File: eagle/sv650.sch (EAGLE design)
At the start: 25 parts

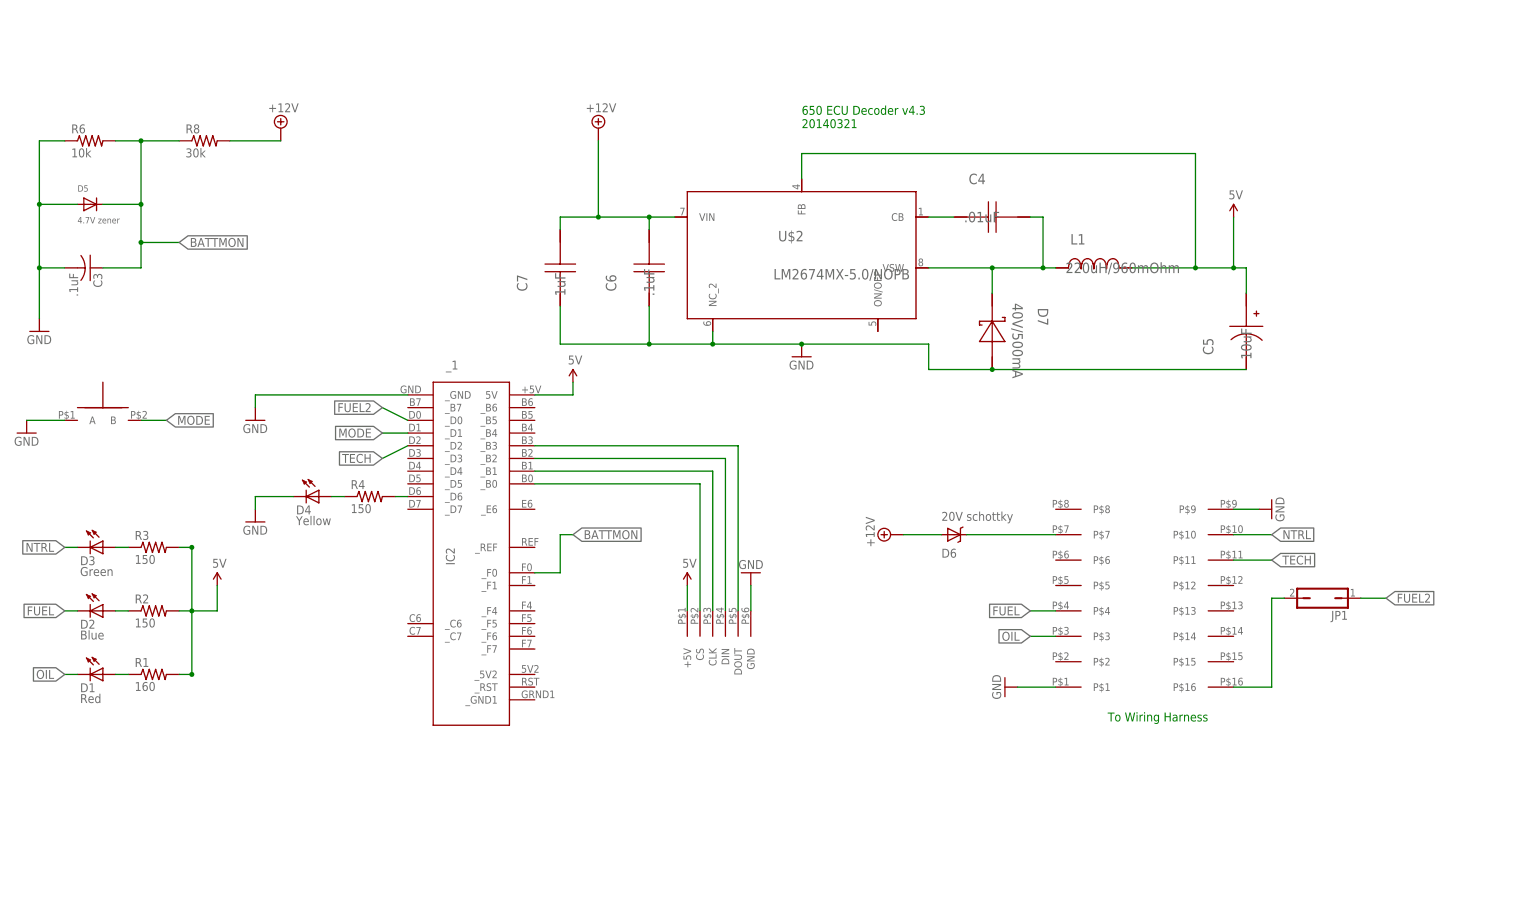
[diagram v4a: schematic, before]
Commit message: Fuel level LED is now controlled by Teensy     Use LT082CP to measure fuel sensor     add 5W 82ohm resistor to fuel line     Remove Fuel2 jumper/support
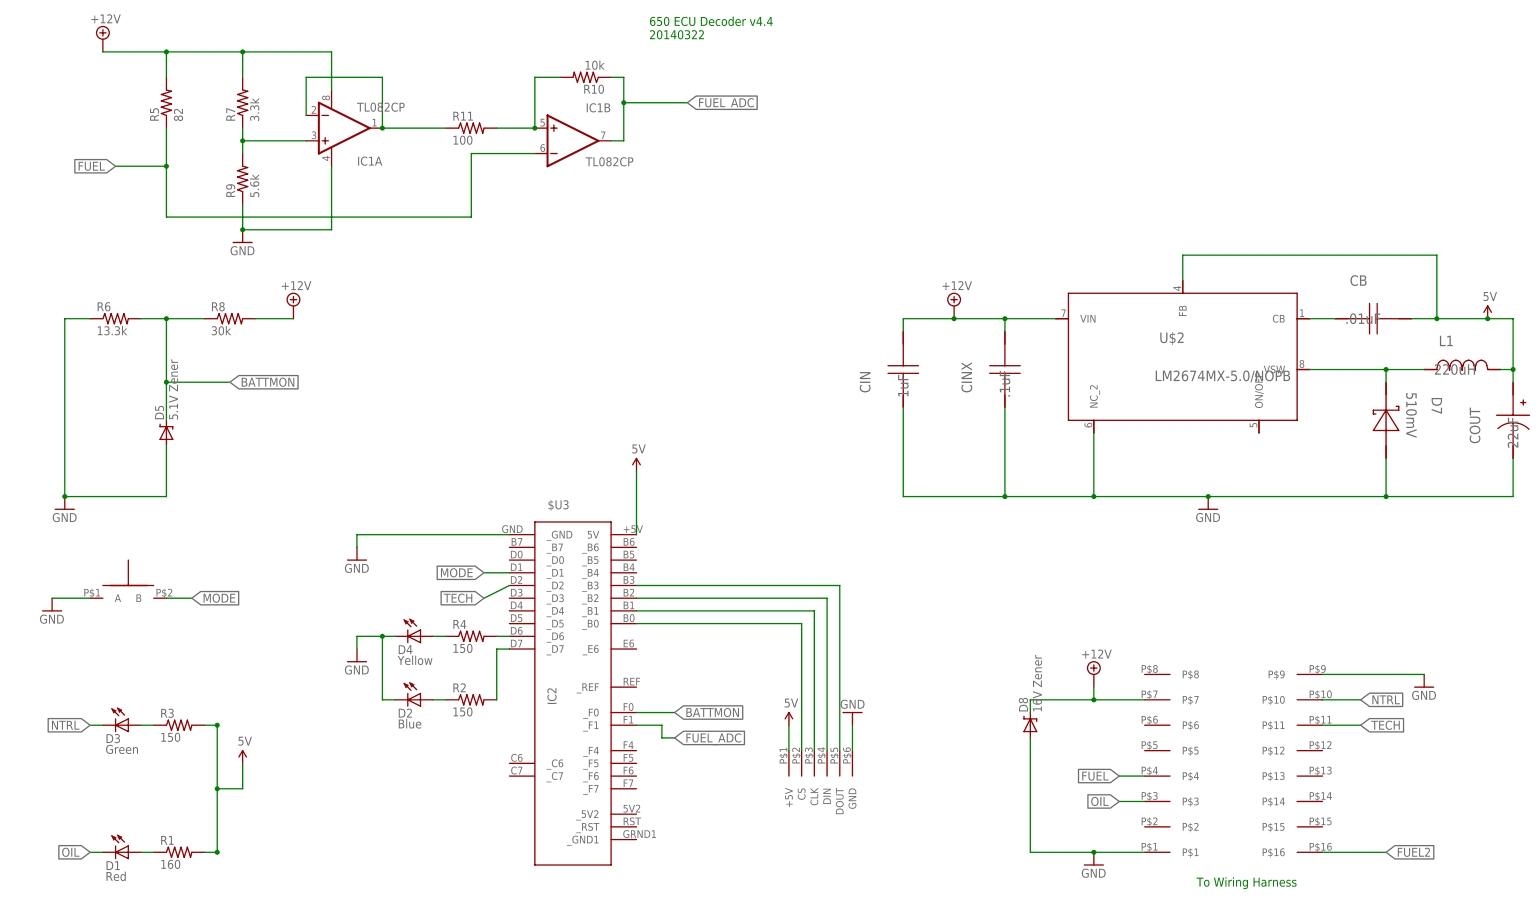
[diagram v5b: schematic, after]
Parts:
- removed C3: .1uF, adafruit:C-US025-024X044
- removed C4: .01uF, TI-LM2674:GRM216R71H103KA01D
- removed C5: 10uF, TI-LM2674:EEE-FK1V100R
- removed C6: .1uF, TI-LM2674:08053C104KAT2A
- removed C7: 1uF, TI-LM2674:C3216X7R1H105K
- removed D6: 20V schottky, synfinatic:SCHOTTKY-DIODESOD-123
- removed JP1: (no value), jumper:JP1Q
- removed _1: IC2, teensy:TEENSY
- added $U3: IC2, teensy:TEENSY
- added CB: .01uF, TI-LM2674:GRM216R71H103KA01D
- added CIN: 1uF, TI-LM2674:GRM219R71E105KA88D
- added CINX: .1uF, TI-LM2674:08053C104KAT2A
- added COUT: 22uF, TI-LM2674:TPSC226K016R0375
- added D8: 16V Zener, SparkFun-DiscreteSemi:DIODE-ZENER-BZT52
- added IC1: TL082CP, SparkFun-AnalogIC:OPAMP-DUALU
- added R10: 10k, synfinatic:RESISTOR0805-RES
- added R11: 100, synfinatic:RESISTOR0805-RES
- added R5: 82, synfinatic:RESISTORPTH-5W
- added R7: 3.3k, synfinatic:RESISTOR0805-RES
- added R9: 5.6k, synfinatic:RESISTOR0805-RES
- D5: value 4.7V zener -> 5.1V Zener; device adafruit:DIODESOD-123 -> SparkFun-DiscreteSemi:DIODE-ZENER-BZT52; MF VISHAY/TELEFUNKEN -> (none); MPN MMSZ5242B-V-GS08 -> (none); OC_NEWARK 35K8677 -> (none)
- D7: value 40V/500mA -> 510mV
- L1: value 220uH/960mOhm -> 220uH
- R6: value 10k -> 13.3k
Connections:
- removed net LOWFUEL2: JP1.2, U$3.P$16
- removed net N$12: D6.C, U$3.P$7
- new net FUEL_ADC: $U3._F1, IC1B.OUT, R10.1
- new net N$15: D7.K, L1.2, U$2.VSW
- new net N$16: $U3._D7, R2.2
- new net N$17: IC1A.+IN, R7.1, R9.2
- new net N$20: IC1B.+IN, R10.2, R11.2
- net +12V: now also CIN.1, CINX.1, D8.C, IC1A.V+, R5.2, R7.2, U$3.P$7; no longer C6.1, C7.1, D6.A
- net 5V: now also $U3.5V, CB.1, COUT.+; no longer C5.+, R2.2, _1.5V
- net BATTMON: now also $U3._F0; no longer C3.1, _1._F0
- net FUEL: now also IC1B.-IN, R5.1; no longer D2.C
- net FUEL2: now also U$3.P$16; no longer JP1.1, _1._D0
- net GND: now also $U3._GND, CIN.2, CINX.2, COUT.-, D2.C, D8.A, IC1A.V-, R9.1; no longer C3.2, C5.-, C6.2, C7.2, _1._GND
- net MODE: now also $U3._D1; no longer _1._D1
- net N$13: now also CB.2; no longer C4.2
- net N$14: now also IC1A.-IN, IC1A.OUT, R11.1; no longer C4.1, D7.K, L1.2, U$2.VSW
- net N$2: now also $U3._B0; no longer _1._B0
- net N$3: now also $U3._B1; no longer _1._B1
- net N$4: now also $U3._B2; no longer _1._B2
- net N$5: now also $U3._B3; no longer _1._B3
- net N$9: now also $U3._D6; no longer _1._D6
- net TECH: now also $U3._D2; no longer _1._D2
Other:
- note added: "650 ECU Decoder v4.4 20140322"
- note removed: "650 ECU Decoder v4.3 20140321"
- moved on the sheet: D1, D2, D3, D4, D7, L1, R1, R2, R3, R4, R6, R8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

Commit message: Replace LM7805 with new Murata 5V switching module Move EFI from D6 to D4 to avoid interrupt conflict Add ground plane Add N channel MOSFET for reverse battery protection Remove 5.1V zener from battery monitor Add 16V zener to clamp +12V line (should move to TVS?) Fix Fuel level circuit for 03-04 and 05+
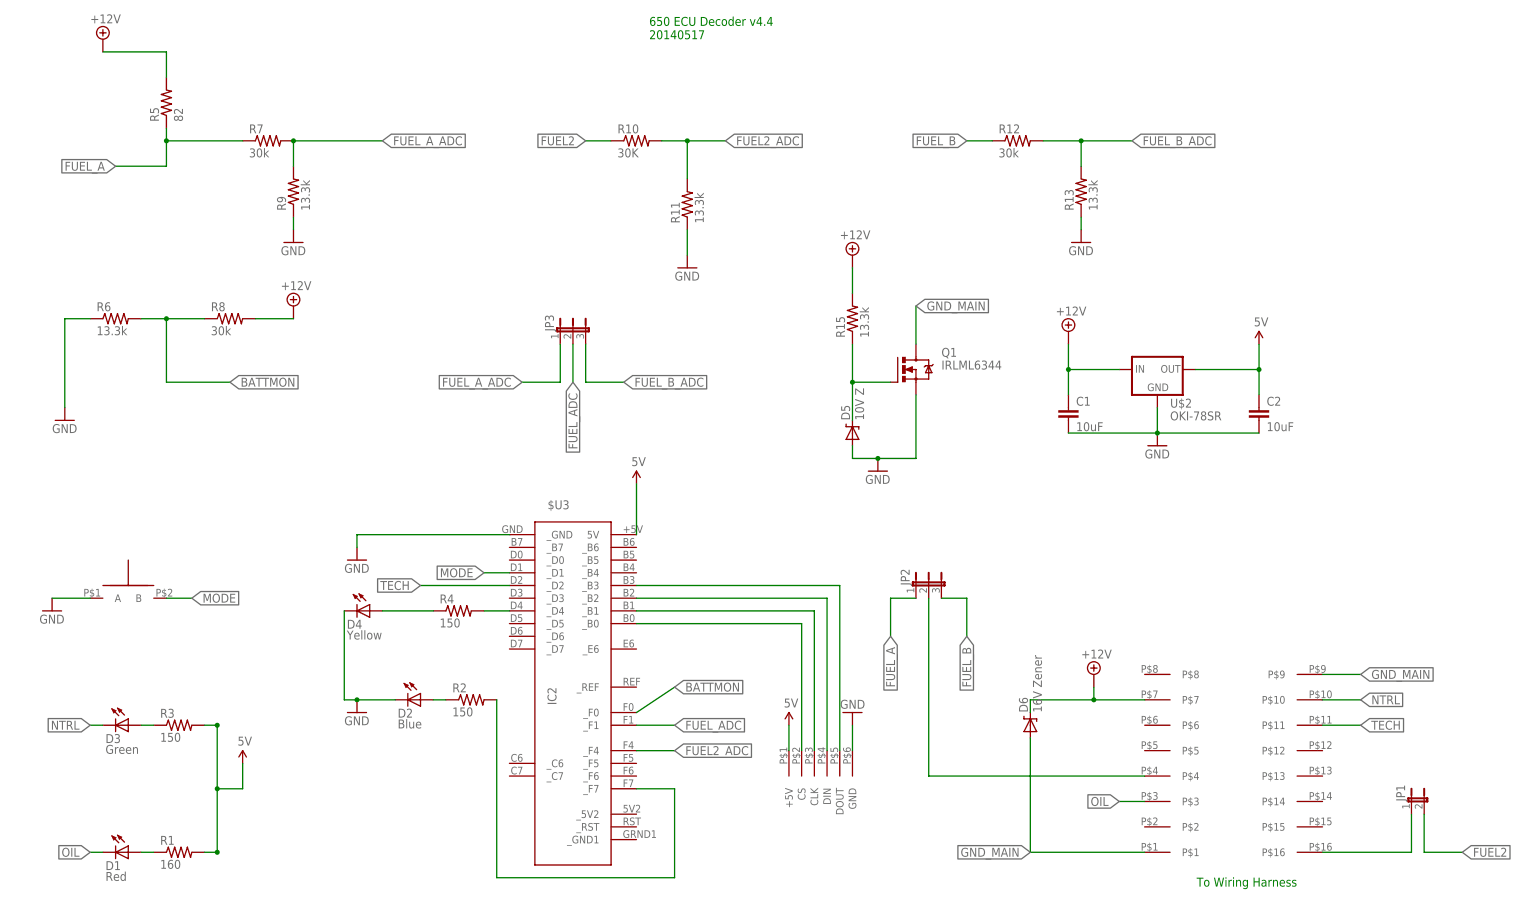
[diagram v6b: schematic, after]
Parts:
- removed CB: .01uF, TI-LM2674:GRM216R71H103KA01D
- removed CIN: 1uF, TI-LM2674:GRM219R71E105KA88D
- removed CINX: .1uF, TI-LM2674:08053C104KAT2A
- removed COUT: 22uF, TI-LM2674:TPSC226K016R0375
- removed D7: 510mV, TI-LM2674:MBR0540T1G
- removed IC1: TL082CP, SparkFun-AnalogIC:OPAMP-DUALU
- removed L1: 220uH, TI-LM2674:SDR0805-221KL
- added C1, C2: 10uF, resistor:C-EUC0805
- added JP1: (no value), jumper:JP1E
- added JP2, JP3: (no value), jumper:JP2E
- added Q1: IRLML6344, synfinatic:IRLML6344
- added R12: 30k, resistor:R-US_M0805
- added R13, R15: 13.3k, resistor:R-US_M0805
- D5: value 5.1V Zener -> 10V Z
- R10: value 10k -> 30K; device synfinatic:RESISTOR0805-RES -> resistor:R-US_M0805
- R11: value 100 -> 13.3k; device synfinatic:RESISTOR0805-RES -> resistor:R-US_M0805
- R7: value 3.3k -> 30k; device synfinatic:RESISTOR0805-RES -> resistor:R-US_M0805
- R9: value 5.6k -> 13.3k; device synfinatic:RESISTOR0805-RES -> resistor:R-US_M0805
- U$2: value LM2674MX-5.0/NOPB -> OKI-78SR; device TI-LM2674:LM2674MX-5.0/NOPB -> synfinatic:OKI-78SR
- renumbered D8 to D6
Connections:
- removed net FUEL: IC1B.-IN, R5.1, U$3.P$4
- removed net N$13: CB.2, U$2.CB
- removed net N$15: D7.K, L1.2, U$2.VSW
- removed net N$20: IC1B.+IN, R10.2, R11.2
- new net FUEL2_ADC: $U3._F4, R10.2, R11.2
- new net FUEL_A: JP2.1, R5.1, R7.1
- new net FUEL_A_ADC: JP3.1, R7.2, R9.2
- new net FUEL_B: JP2.3, R12.1
- new net FUEL_B_ADC: JP3.3, R12.2, R13.2
- new net GND_MAIN: D6.A, Q1.D, U$3.P$1, U$3.P$9
- new net N$12: JP2.2, U$3.P$4
- net +12V: now also C1.1, R15.2, U$2.IN; no longer CIN.1, CINX.1, IC1A.V+, R7.2, U$2.VIN
- net 5V: now also C2.1, U$2.OUT; no longer CB.1, COUT.+, L1.1, U$2.FB
- net BATTMON: no longer D5.C
- net FUEL2: now also JP1.2, R10.1; no longer U$3.P$16
- net FUEL_ADC: now also JP3.2; no longer IC1B.OUT, R10.1
- net GND: now also C1.2, C2.2, Q1.S, R11.1, R13.1, U$2.GND; no longer CIN.2, CINX.2, COUT.-, D6.A, D7.A, IC1A.V-, U$2.NC_2, U$3.P$1, U$3.P$9
- net N$14: now also JP1.1, U$3.P$16; no longer IC1A.-IN, IC1A.OUT, R11.1
- net N$16: now also $U3._F7; no longer $U3._D7
- net N$17: now also D5.C, Q1.G, R15.1; no longer IC1A.+IN, R7.1, R9.2
- net N$9: now also $U3._D4; no longer $U3._D6
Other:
- note added: "650 ECU Decoder v4.4 20140517"
- note removed: "650 ECU Decoder v4.4 20140322"
- moved on the sheet: D4, D5, R10, R11, R4, R7, R9
